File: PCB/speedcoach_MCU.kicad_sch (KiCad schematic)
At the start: 24 parts, among them J3 Conn_01x04_Male, J4 USB_B_Micro, J5 440055-2, SW1 1825027-8, SW2 1825027-8, SW3 1825027-8, U8 MCP73831

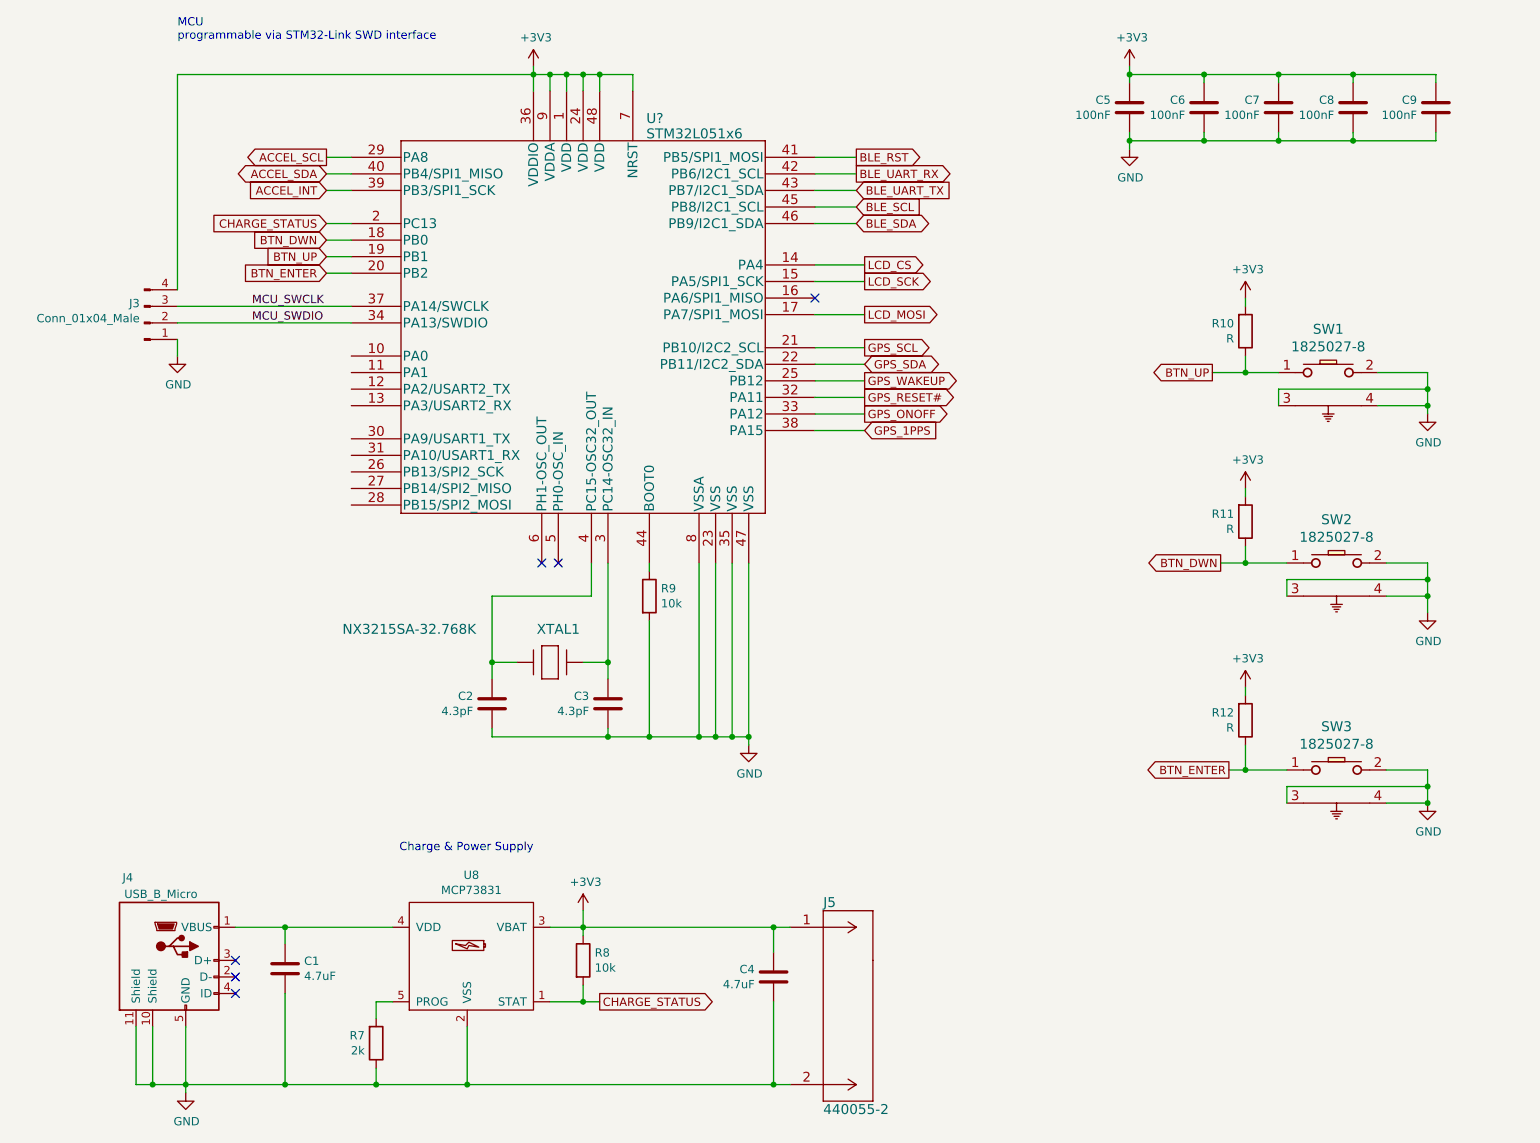
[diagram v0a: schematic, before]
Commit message: added Bluefruit module
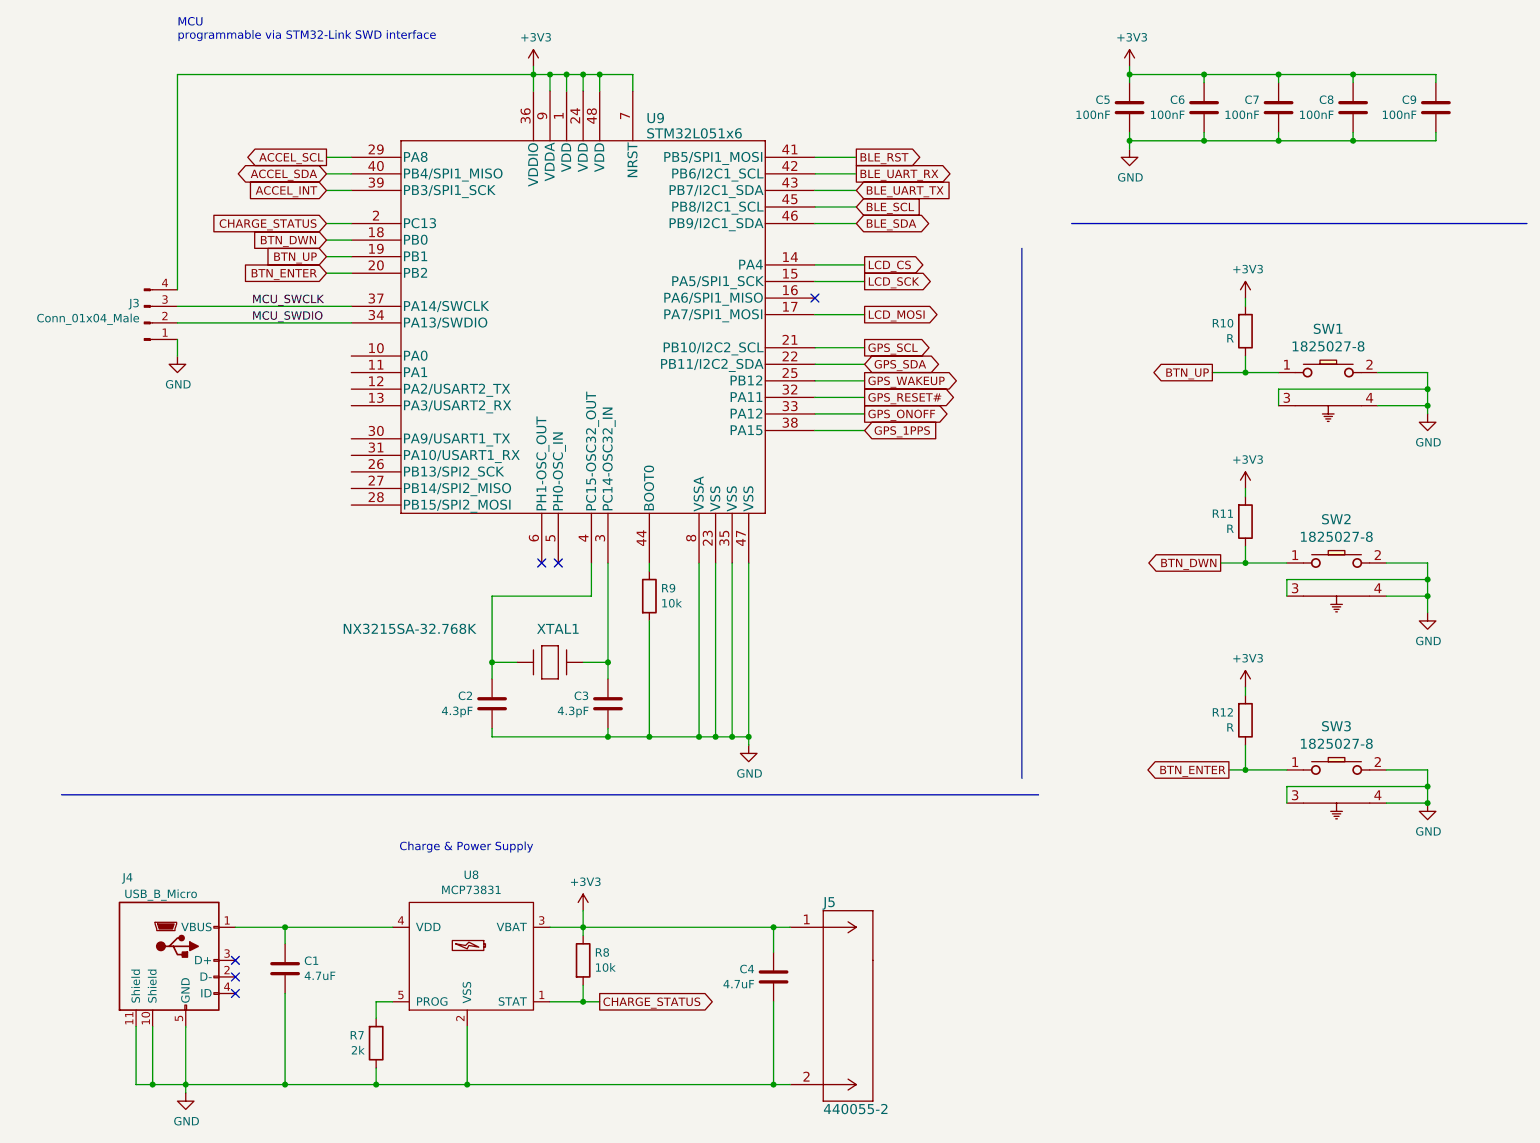
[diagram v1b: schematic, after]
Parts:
- gave numbers to parts that had none: 1
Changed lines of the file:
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@@
+    (stroke (width 0) (type default))
+  )
+  (polyline (pts (xy 189.23 50.8) (xy 259.08 50.8))
     (stroke (width 0) (type default))
   )
@@
     (stroke (width 0) (type default))
   )
+  (polyline (pts (xy 34.29 138.43) (xy 184.15 138.43))
+    (stroke (width 0) (type default))
+  )
   (wire (pts (xy 114.3 30.48) (xy 114.3 27.94))
     (stroke (width 0) (type default))
@@
   )
   (wire (pts (xy 134.62 129.54) (xy 134.62 102.87))
+    (stroke (width 0) (type default))
+  )
+  (polyline (pts (xy 181.61 54.61) (xy 181.61 135.89))
     (stroke (width 0) (type default))
   )
@@
   (symbol (lib_id "speedcoach:STM32L051x6") (at 78.74 40.64 0) (unit 1)
     (in_bom yes) (on_board yes) (fields_autoplaced)
-    (property "Reference" "U?" (id 0) (at 123.9902 34.6738 0)
+    (property "Reference" "U9" (id 0) (at 123.9902 34.6738 0)
       (effects (font (size 1.524 1.524)) (justify left))
     )

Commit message: revised MCU
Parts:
- removed U9: STM32L051x6, speedcoach:STM32L071C8T6, symbol speedcoach:STM32L051x6
- added U9: STM32L051C8T3, symbol speedcoach:STM32L051C8T3
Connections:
- net +3V3: now also U9.1 (VDD), U9.24 (VDD), U9.36 (VDDIO), U9.48 (VDD), U9.7 (NRST), U9.9 (VDDA)
- net ACCEL_INT: now also U9.40 (PB4)
- net BLE_RST: now also U9.39 (PB3)
- net BLE_UART_RX: now also U9.42 (PB6/USART1_TX)
- net BLE_UART_TX: now also U9.43 (PB7/USART1_RX)
- net BTN_DWN: now also U9.18 (PB0)
- net BTN_ENTER: now also U9.20 (PB2)
- net BTN_UP: now also U9.19 (PB1)
- net CHARGE_STATUS: now also U9.2 (PC13)
- net GND: now also U9.23 (VSS), U9.35 (VSS), U9.47 (VSS), U9.8 (VSSA)
- net GPS_1PPS: now also U9.13 (PA3/USART2_RX)
- net GPS_ONOFF: now also U9.12 (PA2/USART2_TX)
- net GPS_RESET#: now also U9.11 (PA1/USART4_RX)
- net GPS_SCL: now also U9.21 (PB10/I2C2_SCL)
- net GPS_SDA: now also U9.22 (PB11/I2C2_SDA)
- net GPS_WAKEUP: now also U9.10 (PA0/USART4_TX)
- net LCD_CS: now also U9.14 (PA4)
- net LCD_MOSI: now also U9.17 (PA7/SPI1_MOSI)
- net LCD_SCK: now also U9.15 (PA5/SPI1_SCK)
- net MCU_SWCLK: now also U9.37 (PA14/SWCLK)
- net MCU_SWDIO: now also U9.34 (PA13/SWDIO)
- net at R9.1: now also U9.44 (BOOT0)
- net at C2.2, XTAL1.1: now also U9.4 (PC15-OSC32_OUT)
- net at C3.2, XTAL1.2: now also U9.3 (PC14-OSC32_IN)
- new net BLE_ACCEL_SCL: U9.45 (PB8/I2C1_SCL)
- new net BLE_ACCEL_SDA: U9.46 (PB9/I2C1_SDA)
- new net BLE_DFU: U9.30 (PA9)
- new net BLE_RTS: U9.31 (PA10)
- new net MEM_CS#: U9.25 (PB12/SPI2_NSS)
- new net MEM_MISO: U9.27 (PB14/SPI2_MISO)
- new net MEM_MOSI: U9.28 (PB15/SPI2_MOSI)
- new net MEM_SCK: U9.26 (PB13/SPI2_SCK)
- no-connect marks 6 -> 11

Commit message: placement
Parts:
- C1, C2, C3, C4, C5, C6, C7, C8, C9: footprint (none) -> Capacitor_SMD:C_0805_2012Metric
- R10, R11, R12: value R -> 3k3; footprint (none) -> Resistor_SMD:R_0805_2012Metric
- R7, R8, R9: footprint (none) -> Resistor_SMD:R_0805_2012Metric
- U9: footprint (none) -> Package_QFP:LQFP-48_7x7mm_P0.5mm
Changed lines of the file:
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@@
       (effects (font (size 1.27 1.27)) (justify right))
     )
-    (property "Footprint" "" (id 2) (at 199.0852 29.21 0)
+    (property "Footprint" "Capacitor_SMD:C_0805_2012Metric" (id 2) (at 199.0852 29.21 0)
       (effects (font (size 1.27 1.27)) hide)
     )
@@
       (effects (font (size 1.27 1.27)) (justify right))
     )
-    (property "Footprint" "" (id 2) (at 210.5152 29.21 0)
+    (property "Footprint" "Capacitor_SMD:C_0805_2012Metric" (id 2) (at 210.5152 29.21 0)
       (effects (font (size 1.27 1.27)) hide)
     )
@@
       (effects (font (size 1.27 1.27)) (justify right))
     )
-    (property "Footprint" "" (id 2) (at 221.9452 29.21 0)
+    (property "Footprint" "Capacitor_SMD:C_0805_2012Metric" (id 2) (at 221.9452 29.21 0)
       (effects (font (size 1.27 1.27)) hide)
     )
@@
       (effects (font (size 1.27 1.27)) (justify right))
     )
-    (property "Footprint" "" (id 2) (at 233.3752 29.21 0)
+    (property "Footprint" "Capacitor_SMD:C_0805_2012Metric" (id 2) (at 233.3752 29.21 0)
       (effects (font (size 1.27 1.27)) hide)
     )
@@
       (effects (font (size 1.27 1.27)) (justify right))
     )
-    (property "Footprint" "" (id 2) (at 246.0752 29.21 0)
+    (property "Footprint" "Capacitor_SMD:C_0805_2012Metric" (id 2) (at 246.0752 29.21 0)
       (effects (font (size 1.27 1.27)) hide)
     )
@@
       (effects (font (size 1.27 1.27)) (justify left))
     )
-    (property "Footprint" "" (id 2) (at 122.682 107.95 90)
+    (property "Footprint" "Resistor_SMD:R_0805_2012Metric" (id 2) (at 122.682 107.95 90)
       (effects (font (size 1.27 1.27)) hide)
     )
@@
       (effects (font (size 1.27 1.27)) (justify left))
     )
-    (property "Footprint" "" (id 2) (at 69.5452 168.91 0)
+    (property "Footprint" "Capacitor_SMD:C_0805_2012Metric" (id 2) (at 69.5452 168.91 0)
       (effects (font (size 1.27 1.27)) hide)
     )
@@
       (effects (font (size 1.27 1.27)) (justify right))
     )
-    (property "Footprint" "" (id 2) (at 80.772 176.53 90)
+    (property "Footprint" "Resistor_SMD:R_0805_2012Metric" (id 2) (at 80.772 176.53 90)
       (effects (font (size 1.27 1.27)) hide)
     )
@@
       (effects (font (size 1.27 1.27)) (justify left))
     )
-    (property "Footprint" "" (id 2) (at 112.522 163.83 90)
+    (property "Footprint" "Resistor_SMD:R_0805_2012Metric" (id 2) (at 112.522 163.83 90)
       (effects (font (size 1.27 1.27)) hide)
     )
@@
       (effects (font (size 1.27 1.27)) (justify right))
     )
-    (property "Footprint" "" (id 2) (at 144.4752 162.56 0)
+    (property "Footprint" "Capacitor_SMD:C_0805_2012Metric" (id 2) (at 144.4752 162.56 0)
       (effects (font (size 1.27 1.27)) hide)
     )
@@
       (effects (font (size 1.27 1.27)) (justify right))
     )
-    (property "Value" "R" (id 1) (at 214.1474 68.453 0)
-      (effects (font (size 1.27 1.27)) (justify right))
-    )
-    (property "Footprint" "" (id 2) (at 214.122 67.31 90)
+    (property "Value" "3k3" (id 1) (at 214.1474 68.453 0)
+      (effects (font (size 1.27 1.27)) (justify right))
+    )
+    (property "Footprint" "Resistor_SMD:R_0805_2012Metric" (id 2) (at 214.122 67.31 90)
       (effects (font (size 1.27 1.27)) hide)
     )
@@
       (effects (font (size 1.27 1.27)) (justify right))
     )
-    (property "Value" "R" (id 1) (at 214.1474 97.663 0)
-      (effects (font (size 1.27 1.27)) (justify right))
-    )
-    (property "Footprint" "" (id 2) (at 214.122 96.52 90)
+    (property "Value" "3k3" (id 1) (at 214.1474 97.663 0)
+      (effects (font (size 1.27 1.27)) (justify right))
+    )
+    (property "Footprint" "Resistor_SMD:R_0805_2012Metric" (id 2) (at 214.122 96.52 90)
       (effects (font (size 1.27 1.27)) hide)
     )
@@
       (effects (font (size 1.27 1.27)) (justify right))
     )
-    (property "Value" "R" (id 1) (at 214.1474 128.143 0)
-      (effects (font (size 1.27 1.27)) (justify right))
-    )
-    (property "Footprint" "" (id 2) (at 214.122 127 90)
+    (property "Value" "3k3" (id 1) (at 214.1474 128.143 0)
+      (effects (font (size 1.27 1.27)) (justify right))
+    )
+    (property "Footprint" "Resistor_SMD:R_0805_2012Metric" (id 2) (at 214.122 127 90)
       (effects (font (size 1.27 1.27)) hide)
     )
@@
       (effects (font (size 1.27 1.27)) (justify right))
     )
-    (property "Footprint" "" (id 2) (at 101.2952 120.65 0)
+    (property "Footprint" "Capacitor_SMD:C_0805_2012Metric" (id 2) (at 101.2952 120.65 0)
       (effects (font (size 1.27 1.27)) hide)
     )
@@
       (effects (font (size 1.27 1.27)) (justify right))
     )
-    (property "Footprint" "" (id 2) (at 119.0752 120.65 0)
+    (property "Footprint" "Capacitor_SMD:C_0805_2012Metric" (id 2) (at 119.0752 120.65 0)
       (effects (font (size 1.27 1.27)) hide)
     )
@@
       (effects (font (size 1.524 1.524)) (justify left))
     )
-    (property "Footprint" "" (id 2) (at 52.07 26.67 0)
-      (effects (font (size 1.524 1.524)) hide)
-    )
+    (property "Footprint" "Package_QFP:LQFP-48_7x7mm_P0.5mm" (id 2) (at 52.07 26.67 0)
+      (effects (font (size 1.524 1.524)) hide)
+    )
